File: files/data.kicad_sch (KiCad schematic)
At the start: 16 parts, among them U1 86C325

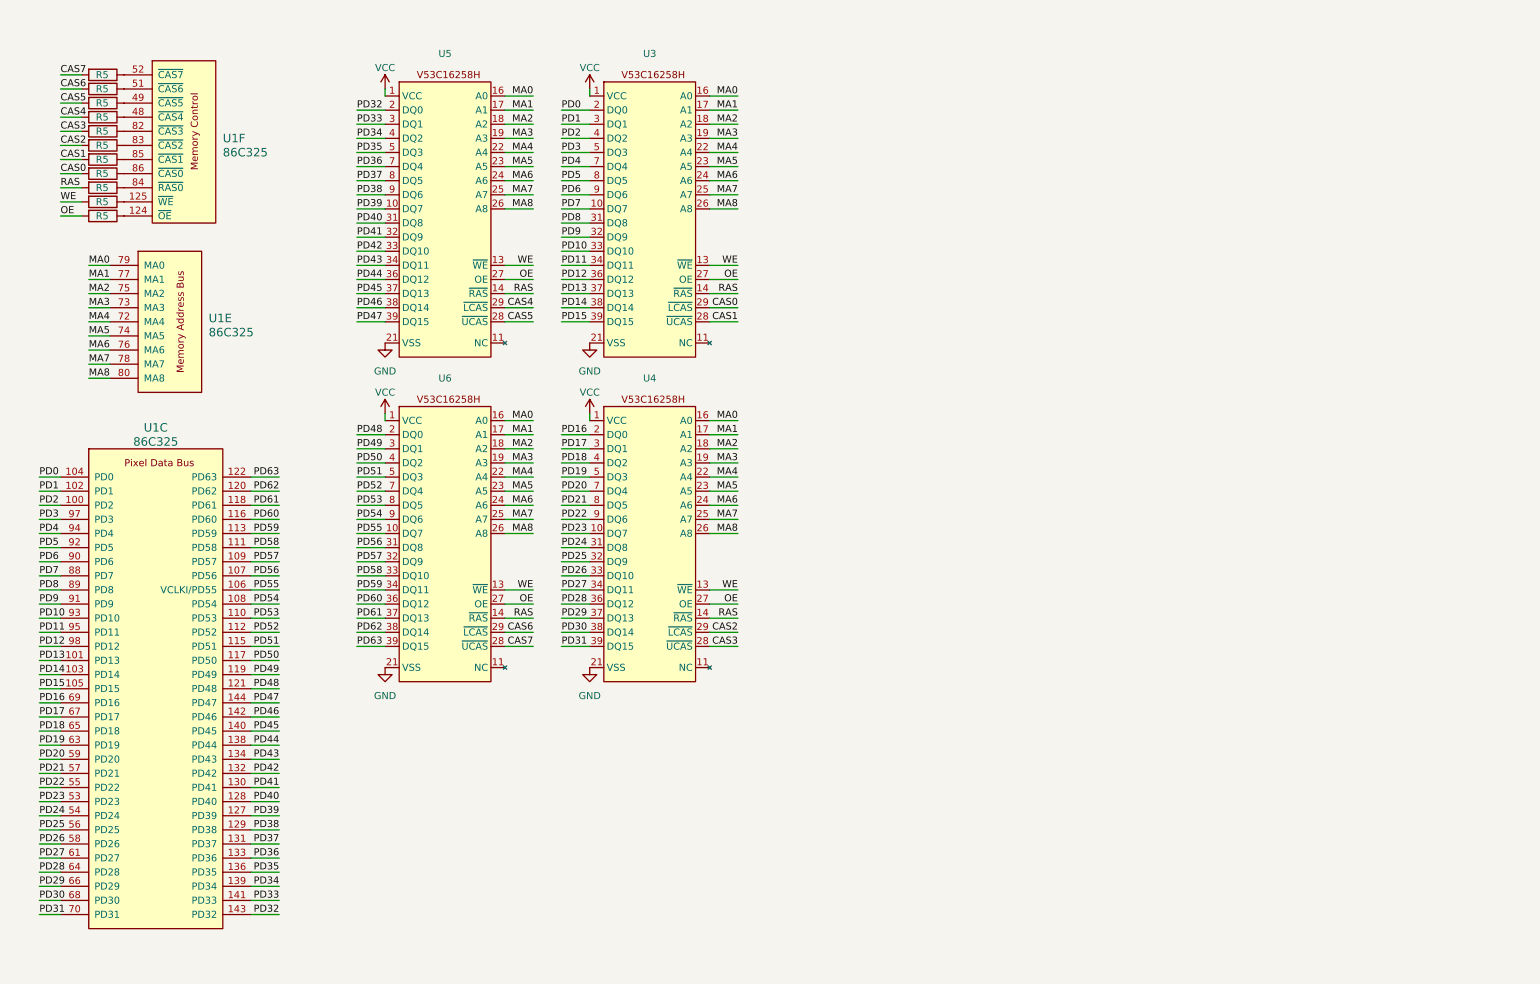
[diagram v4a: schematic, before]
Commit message: added register strap resistors
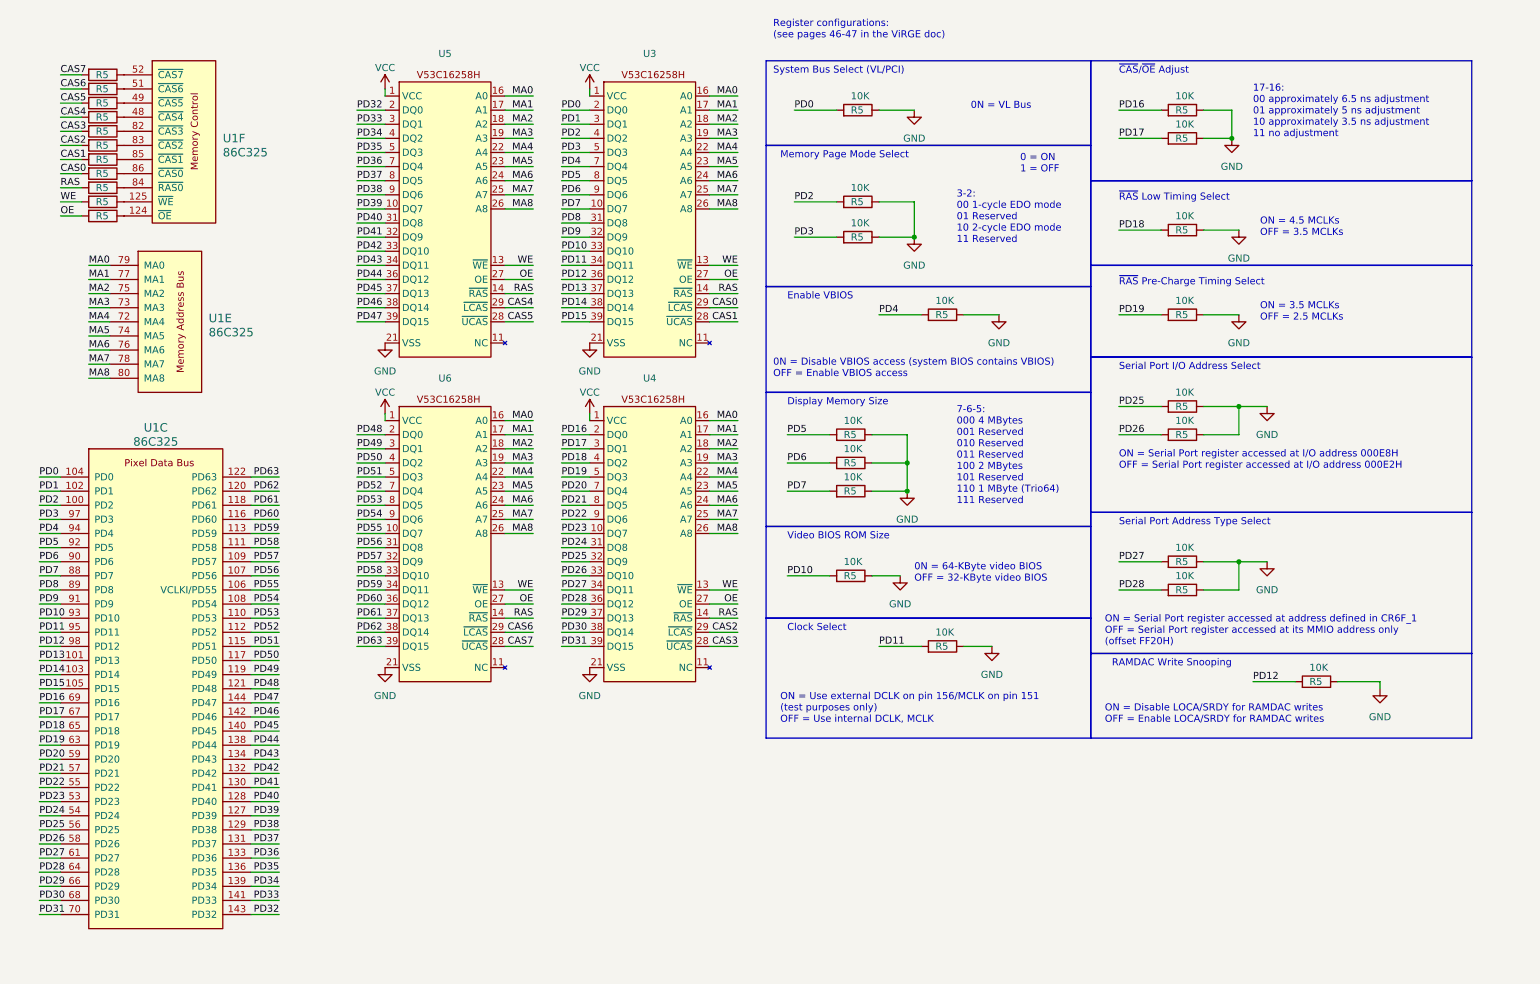
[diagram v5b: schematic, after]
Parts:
- added R5 (x18): 10K, Resistor_SMD:R_0805_2012Metric_Pad1.20x1.40mm_HandSolder, symbol Device:R
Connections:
- net GND: now also R5.1, R5.1, R5.1, R5.1, R5.1, R5.1, R5.1, R5.1, R5.1, R5.1, R5.1, R5.1, R5.1, R5.1, R5.1, R5.1, R5.1, R5.1
- net PD0: now also R5.2
- net PD10: now also R5.2
- net PD11: now also R5.2
- net PD12: now also R5.2
- net PD16: now also R5.2
- net PD17: now also R5.2
- net PD18: now also R5.2
- net PD19: now also R5.2
- net PD2: now also R5.2
- net PD25: now also R5.2
- net PD26: now also R5.2
- net PD27: now also R5.2
- net PD28: now also R5.2
- net PD3: now also R5.2
- net PD4: now also R5.2
- net PD5: now also R5.2
- net PD6: now also R5.2
- net PD7: now also R5.2
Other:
- note added: "0 = ON 1 = OFF"
- note added: "0N = 64-KByte video BIOS OFF = 32-KByte video BIOS"
- note added: "0N = Disable VBIOS access (system BIOS contains VBIOS) OFF = Enable VBIOS access"
- note added: "0N = VL Bus"
- note added: "17-16: 00 approximately 6.5 ns adjustment 01 approximately 5 ns adjustment 10 approximately 3.5 ns adjustment 11 no adjustment"
- note added: "3-2: 00 1-cycle EDO mode 01 Reserved 10 2-cycle EDO mode 11 Reserved"
- note added: "7-6-5: 000 4 MBytes 001 Reserved 010 Reserved 011 Reserved 100 2 MBytes 101 Reserved 110 1 MByte (Trio64) 111 Reserved"
- note added: "Clock Select"
- note added: "Display Memory Size"
- note added: "Enable VBIOS"
- note added: "Memory Page Mode Select"
- note added: "ON = 3.5 MCLKs OFF = 2.5 MCLKs"
- note added: "ON = 4.5 MCLKs OFF = 3.5 MCLKs"
- note added: "ON = Disable LOCA/SRDY for RAMDAC writes OFF = Enable LOCA/SRDY for RAMDAC writes"
- note added: "ON = Serial Port register accessed at I/O address 000E8H OFF = Serial Port register accessed at I/O address 000E2H"
- note added: "ON = Serial Port register accessed at address defined in CR6F_1 OFF = Serial Port register accessed at its MMIO address only (offset FF20H)"
- note added: "ON = Use external DCLK on pin 156/MCLK on pin 151 (test purposes only) OFF = Use internal DCLK, MCLK"
- note added: "RAMDAC Write Snooping"
- note added: "Register configurations: (see pages 46-47 in the ViRGE doc)"
- note added: "Serial Port Address Type Select"
- note added: "Serial Port I/O Address Select"
- note added: "System Bus Select (VL/PCI)"
- note added: "Video BIOS ROM Size"
- note added: "~{CAS}/~{OE} Adjust"
- note added: "~{RAS} Low Timing Select"
- note added: "~{RAS} Pre-Charge Timing Select"

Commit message: added SAUP decoding, adjusted VGA conn.
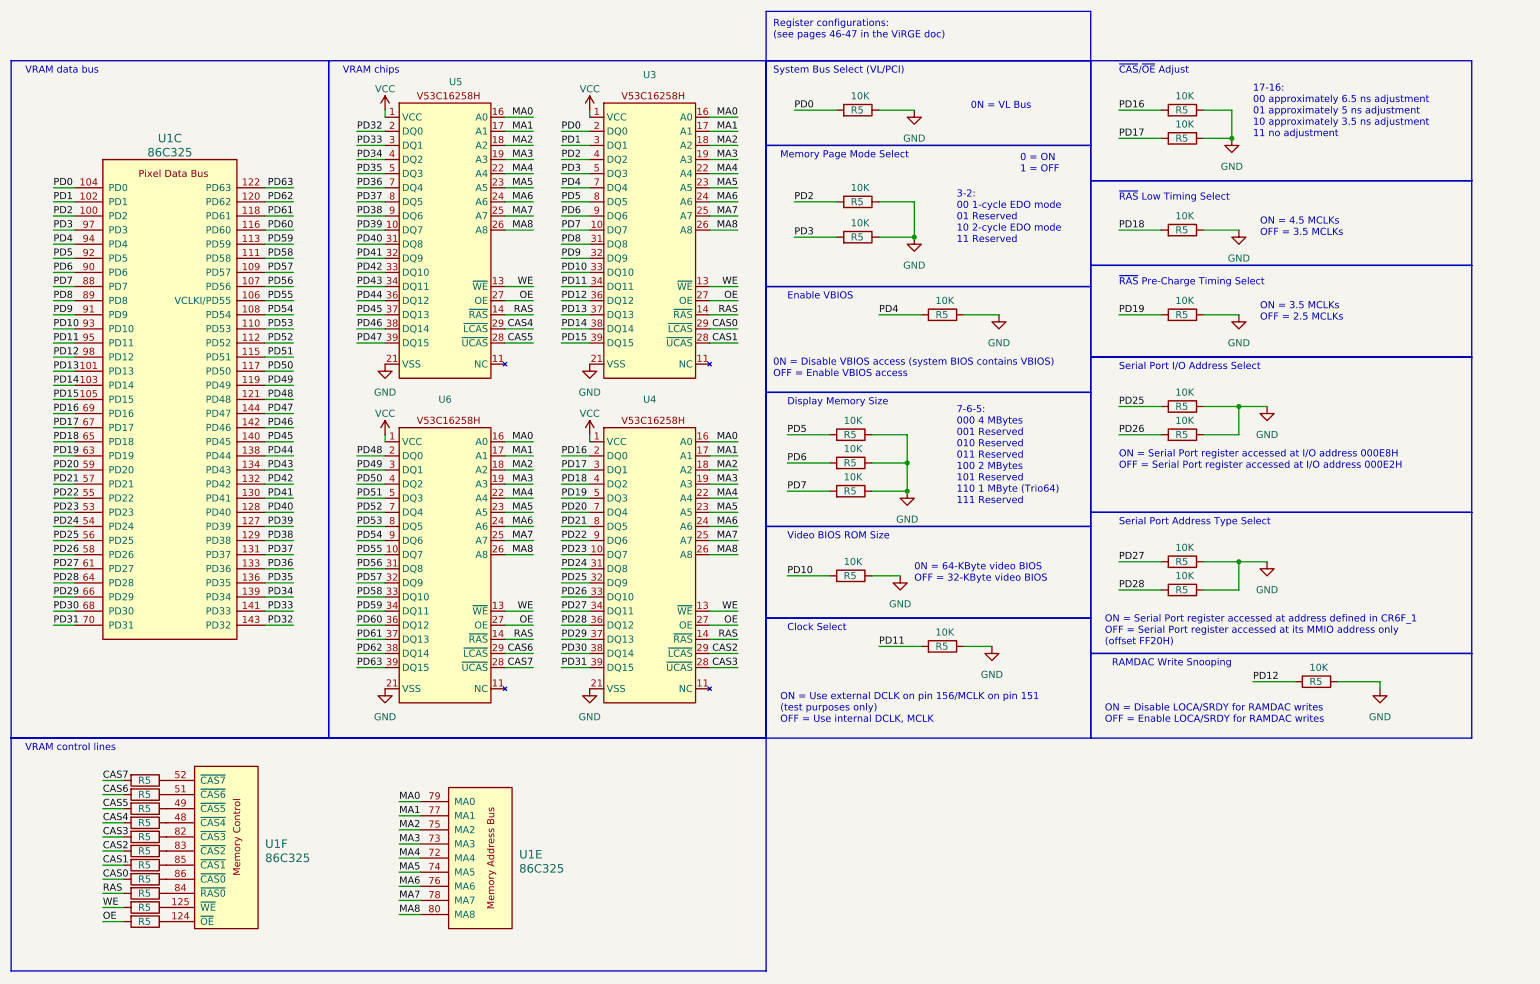
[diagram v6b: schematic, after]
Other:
- note added: "VRAM chips"
- note added: "VRAM control lines"
- note added: "VRAM data bus"
- moved on the sheet: R5, U1C, U1E, U1F, U3, U4, U5, U6

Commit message: Board review changes 2023-07-06
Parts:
- R5: Installed (none) -> 1
- R5: Installed (none) -> 0
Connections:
- no-connect marks 0 -> 4
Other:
- note added: "Default 2 WS Install PD27, NO PD28"
- note added: "ON = 0 = Pull Down OFF = 1 = Open"
- note added: "PD16 = R45 PD17 = R46"
- note added: "PD25 LOW = CR I/O address 000E8H PD25 HIGH = CR I/O address 000E2H PD26 LOW = Serial CR IO E2H/E8H PD26 HIGH = MMIO Address window IO"
- note added: "PD5 = R40 PD6 = R41 PD7 = R42"
- note added: "PD: 7-6-5: 000 4 MBytes 001 Reserved 010 Reserved 011 Reserved 100 2 MBytes 101 Reserved 110 1 MByte (Trio64) 111 Reserved"
- note added: "Serial Port I/O Address & Type Select"
- note added: "WE Delay | PD28 | PD27 | 3 units | 0 | 0 | 2 units | 0 | 1 | 1 units | 1 | 0 | 0 units | 1 | 1 |"
- note removed: "0 = ON 1 = OFF"
- note removed: "7-6-5: 000 4 MBytes 001 Reserved 010 Reserved 011 Reserved 100 2 MBytes 101 Reserved 110 1 MByte (Trio64) 111 Reserved"
- note removed: "ON = Serial Port register accessed at I/O address 000E8H OFF = Serial Port register accessed at I/O address 000E2H"
- note removed: "ON = Serial Port register accessed at address defined in CR6F_1 OFF = Serial Port register accessed at its MMIO address only (offset FF20H)"
- note removed: "Serial Port Address Type Select"
- note removed: "Serial Port I/O Address Select"
- moved on the sheet: R5, U1E, U1F

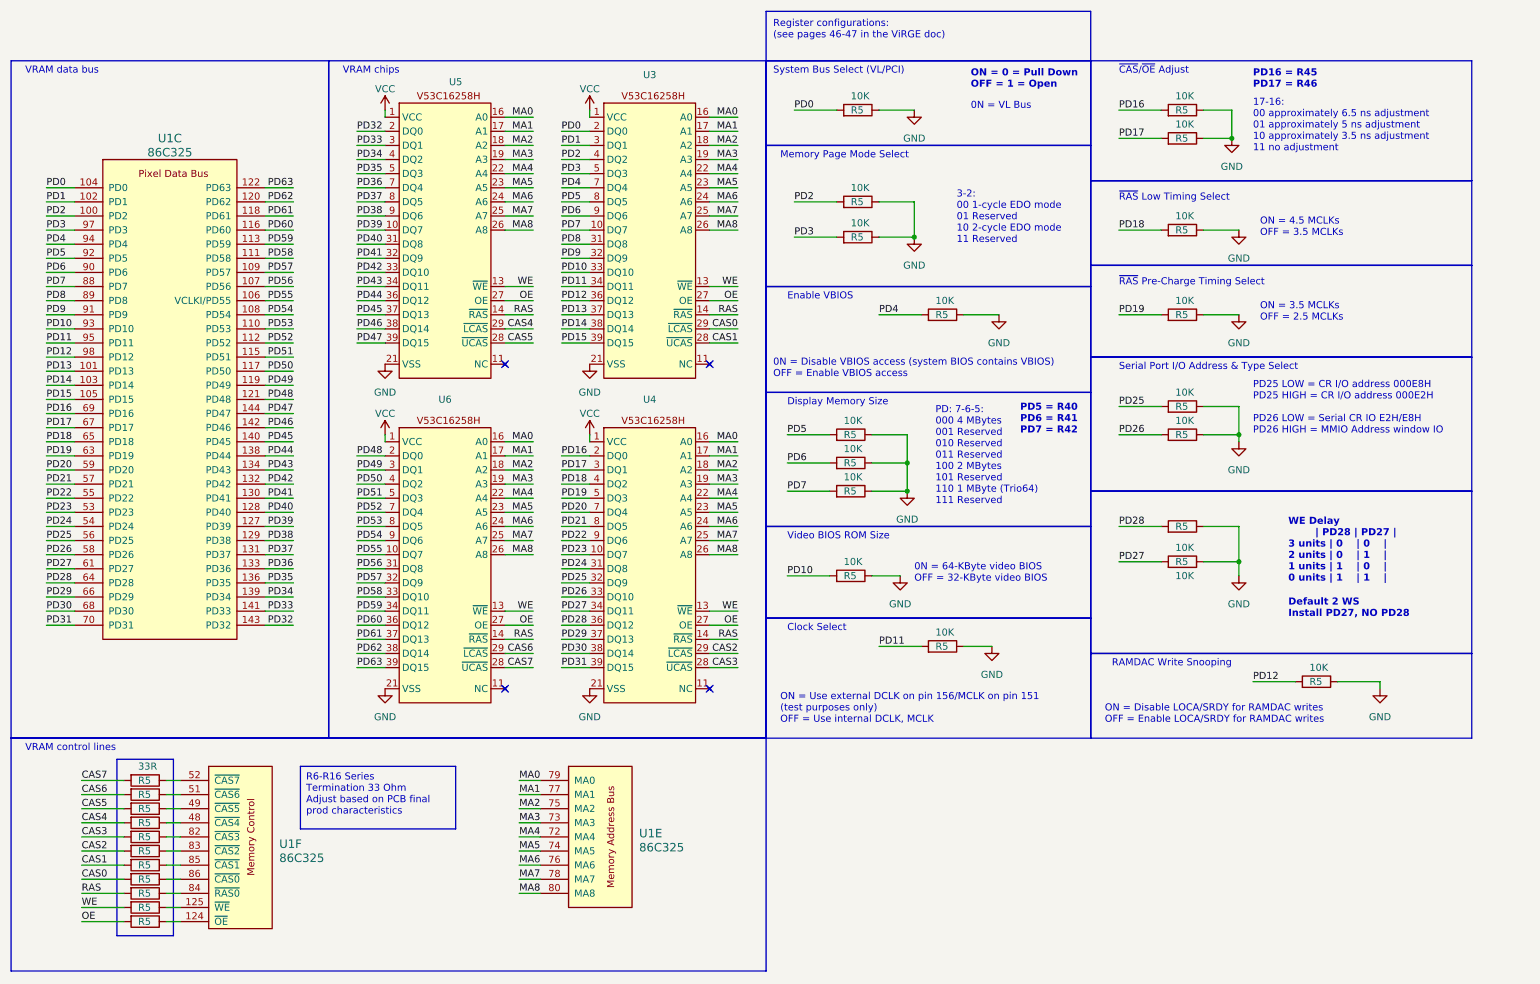
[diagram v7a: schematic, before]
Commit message: fixed some clearance issues, fixed S3 logo, fixed annotations
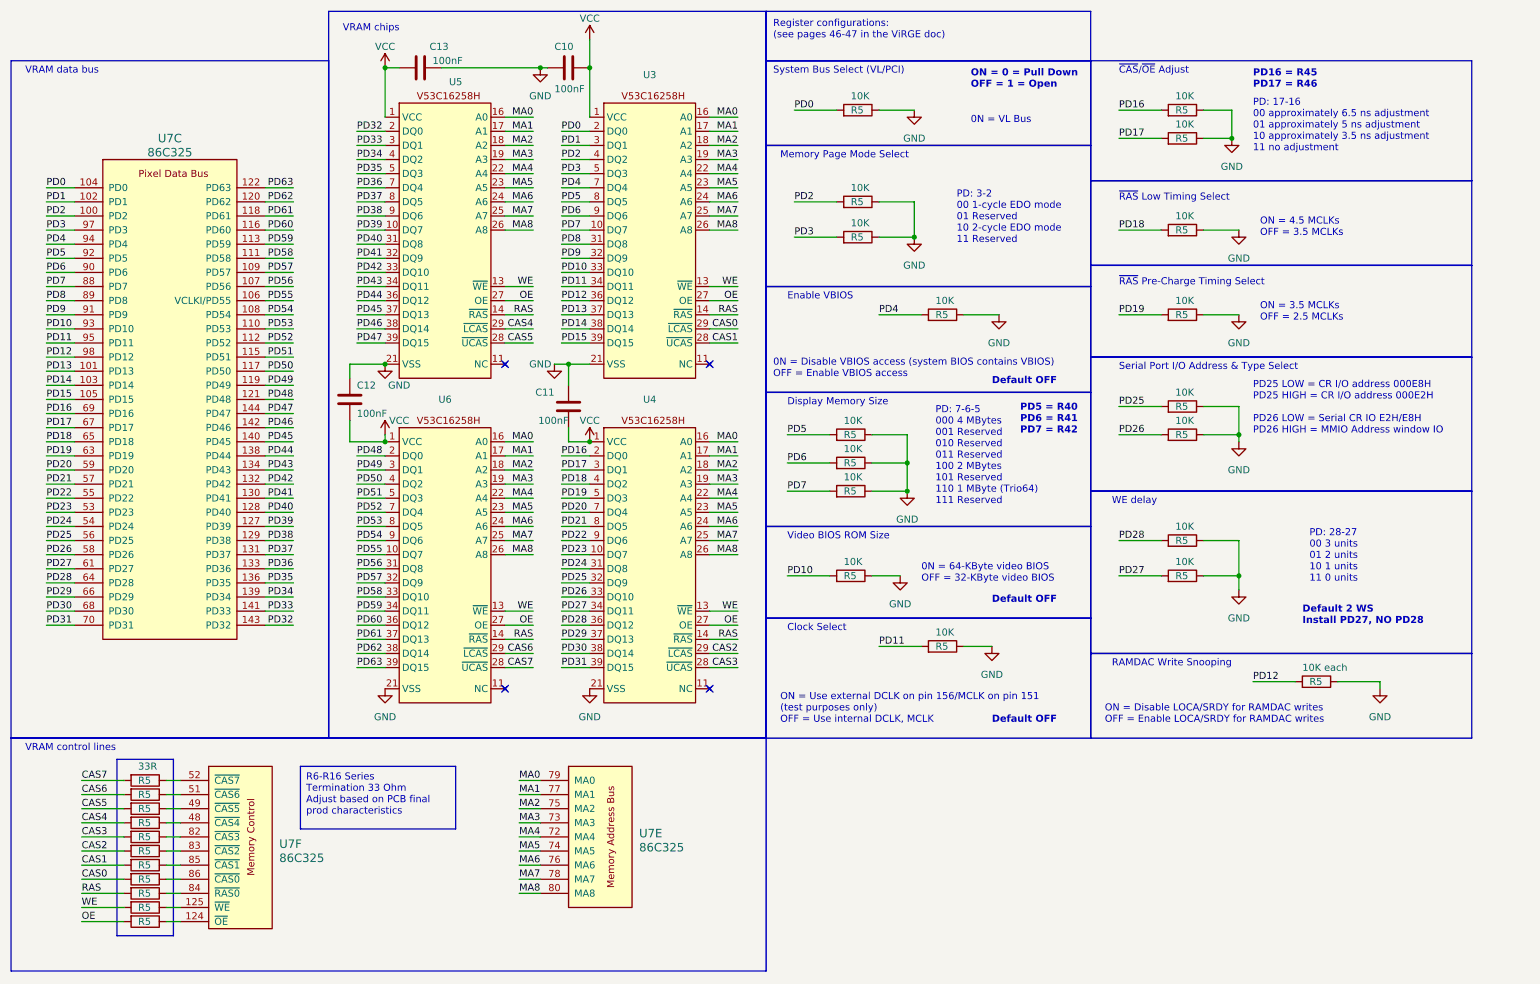
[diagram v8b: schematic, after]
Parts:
- added C10, C11, C12, C13: 100nF, Capacitor_SMD:C_0805_2012Metric_Pad1.18x1.45mm_HandSolder, symbol Device:C
- R5: value 10K -> 10K each
- R5: value 33R -> 3 x 33R
- renumbered U1 to U7
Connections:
- net GND: now also C10.2, C11.2, C12.1, C13.2
- net VCC: now also C10.1, C11.1, C12.2, C13.1
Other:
- note added: "Default OFF"
- note added: "PD: 17-16 00 approximately 6.5 ns adjustment 01 approximately 5 ns adjustment 10 approximately 3.5 ns adjustment 11 no adjustment"
- note added: "PD: 28-27 00 3 units 01 2 units 10 1 units 11 0 units"
- note added: "PD: 3-2 00 1-cycle EDO mode 01 Reserved 10 2-cycle EDO mode 11 Reserved"
- note added: "PD: 7-6-5 000 4 MBytes 001 Reserved 010 Reserved 011 Reserved 100 2 MBytes 101 Reserved 110 1 MByte (Trio64) 111 Reserved"
- note added: "WE delay"
- note removed: "17-16: 00 approximately 6.5 ns adjustment 01 approximately 5 ns adjustment 10 approximately 3.5 ns adjustment 11 no adjustment"
- note removed: "3-2: 00 1-cycle EDO mode 01 Reserved 10 2-cycle EDO mode 11 Reserved"
- note removed: "PD: 7-6-5: 000 4 MBytes 001 Reserved 010 Reserved 011 Reserved 100 2 MBytes 101 Reserved 110 1 MByte (Trio64) 111 Reserved"
- note removed: "WE Delay | PD28 | PD27 | 3 units | 0 | 0 | 2 units | 0 | 1 | 1 units | 1 | 0 | 0 units | 1 | 1 |"
- moved on the sheet: R5
